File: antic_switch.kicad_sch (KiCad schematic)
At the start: 10 parts, among them J1 2.54, J2 2.00, P1 ANTIC_Conn, SW2 SW_Push_SPDT, U1 ANTIC_NTSC, U2 74LS245, U3 ANTIC_PAL, U4 74LS245

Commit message: gerber
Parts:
- SW2: now left out of the parts list
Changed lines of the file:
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@@
 		(unit 1)
 		(exclude_from_sim no)
-		(in_bom yes)
-		(on_board yes)
+		(in_bom no)
+		(on_board no)
 		(dnp no)
 		(property "Reference" "SW2"

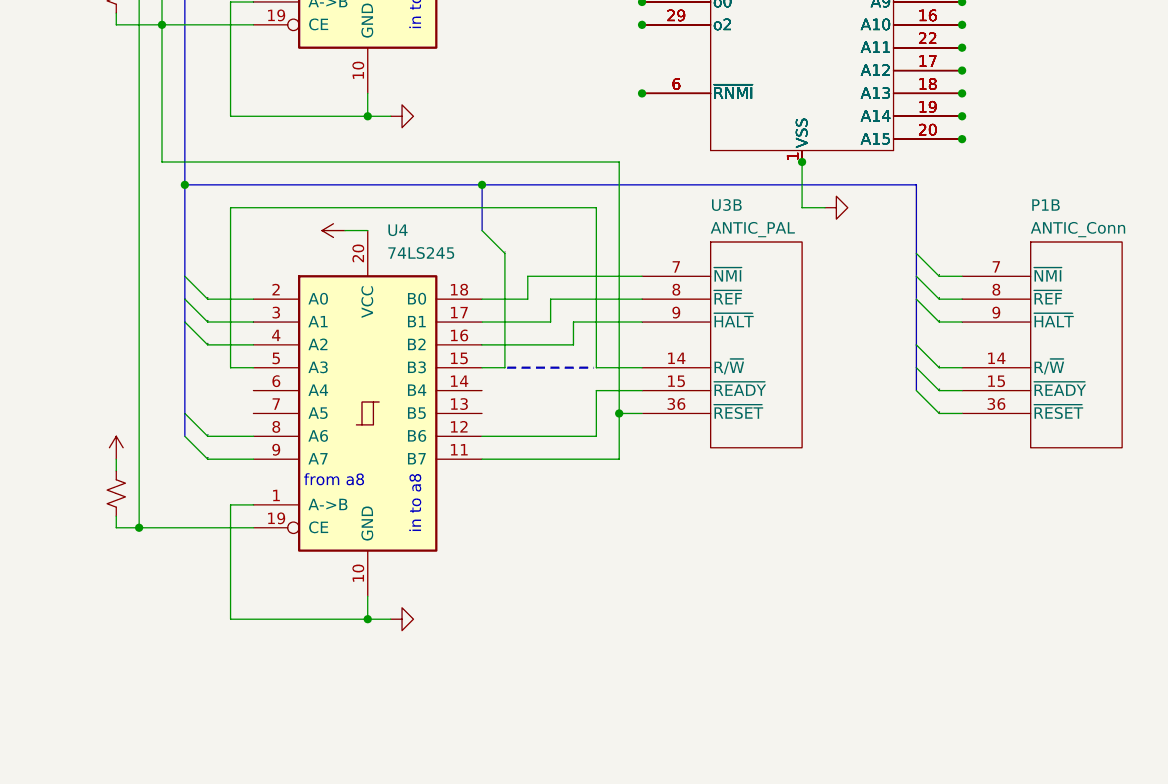
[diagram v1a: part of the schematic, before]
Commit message: header for gtia clocks
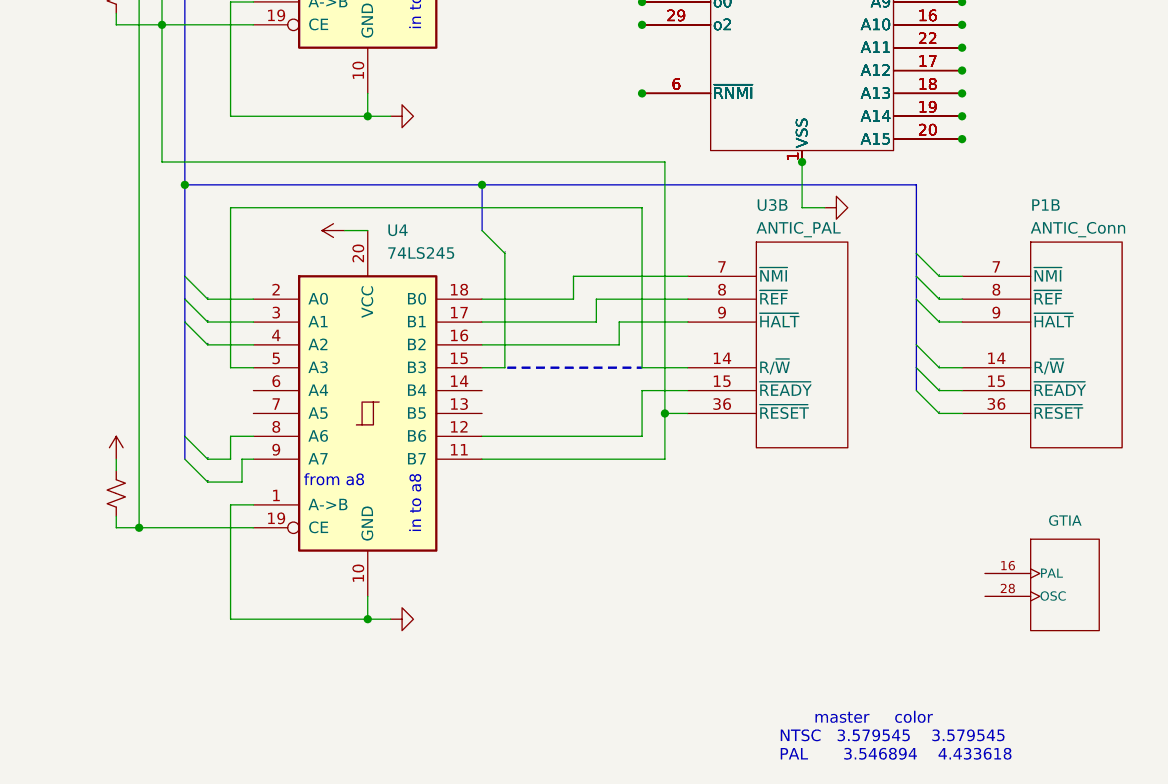
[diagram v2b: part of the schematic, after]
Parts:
- added IC2: GTIA, Package_DIP:DIP-40_W15.24mm, symbol Atari8:GTIA
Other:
- note added: "master color NTSC 3.579545 3.579545 PAL 3.546894 4.433618"
- moved on the sheet: U3B
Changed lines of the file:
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@@
 		)
 	)
+	(text "	   master 	color\nNTSC   3.579545	3.579545\nPAL	   3.546894	4.433618"
+		(exclude_from_sim no)
+		(at 177.8 157.734 0)
+		(effects
+			(font
+				(size 1.27 1.27)
+			)
+			(justify left top)
+		)
+	)
 	(text "in to a8"
 		(exclude_from_sim no)
@@
 	)
 	(junction
-		(at 160.02 124.46)
+		(at 165.1 124.46)
 		(diameter 0)
 		(color 0 0 0 0)
@@
 	)
 	(bus_entry
-		(at 111.76 124.46)
+		(at 111.76 127)
 		(size 2.54 2.54)
 		(stroke
@@
 	)
 	(bus_entry
-		(at 111.76 127)
+		(at 111.76 129.54)
 		(size 2.54 2.54)
 		(stroke
@@
 	(wire
 		(pts
-			(xy 152.4 114.3) (xy 144.78 114.3)
+			(xy 157.48 114.3) (xy 144.78 114.3)
 		)
 		(stroke
@@
 	(wire
 		(pts
-			(xy 157.48 101.6) (xy 116.84 101.6)
+			(xy 162.56 101.6) (xy 116.84 101.6)
 		)
 		(stroke
@@
 	(bus
 		(pts
-			(xy 111.76 114.3) (xy 111.76 124.46)
+			(xy 111.76 114.3) (xy 111.76 127)
 		)
 		(stroke
@@
 	(wire
 		(pts
-			(xy 154.94 116.84) (xy 144.78 116.84)
+			(xy 160.02 116.84) (xy 144.78 116.84)
 		)
 		(stroke
@@
 	(wire
 		(pts
-			(xy 160.02 96.52) (xy 160.02 124.46)
+			(xy 165.1 96.52) (xy 165.1 124.46)
 		)
 		(stroke
@@
 	(wire
 		(pts
-			(xy 157.48 119.38) (xy 162.56 119.38)
+			(xy 162.56 119.38) (xy 167.64 119.38)
 		)
 		(stroke
@@
 	(wire
 		(pts
-			(xy 160.02 129.54) (xy 160.02 124.46)
+			(xy 165.1 129.54) (xy 165.1 124.46)
 		)
 		(stroke
@@
 	(polyline
 		(pts
-			(xy 147.574 119.38) (xy 157.226 119.38)
+			(xy 147.574 119.38) (xy 162.56 119.38)
 		)
 		(stroke
@@
 	(wire
 		(pts
-			(xy 157.48 127) (xy 157.48 121.92)
+			(xy 162.56 127) (xy 162.56 121.92)
 		)
 		(stroke
@@
 	(wire
 		(pts
-			(xy 157.48 121.92) (xy 162.56 121.92)
+			(xy 162.56 121.92) (xy 167.64 121.92)
 		)
 		(stroke
@@
 	(wire
 		(pts
+			(xy 118.11 129.54) (xy 119.38 129.54)
+		)
+		(stroke
+			(width 0)
+			(type default)
+		)
+	)
+	(wire
+		(pts
 			(xy 144.78 63.5) (xy 147.32 63.5)
 		)
@@
 	(wire
 		(pts
-			(xy 157.48 119.38) (xy 157.48 101.6)
+			(xy 162.56 119.38) (xy 162.56 101.6)
 		)
 		(stroke
@@
 	(wire
 		(pts
-			(xy 114.3 127) (xy 119.38 127)
+			(xy 114.3 129.54) (xy 116.84 129.54)
 		)
 		(stroke
@@
 	(bus
 		(pts
-			(xy 111.76 124.46) (xy 111.76 127)
+			(xy 111.76 127) (xy 111.76 129.54)
 		)
 		(stroke
@@
 	(wire
 		(pts
-			(xy 162.56 111.76) (xy 152.4 111.76)
+			(xy 167.64 111.76) (xy 157.48 111.76)
 		)
 		(stroke
@@
 	(wire
 		(pts
-			(xy 152.4 111.76) (xy 152.4 114.3)
+			(xy 157.48 111.76) (xy 157.48 114.3)
 		)
 		(stroke
@@
 	(wire
 		(pts
-			(xy 144.78 127) (xy 157.48 127)
+			(xy 144.78 127) (xy 162.56 127)
 		)
 		(stroke
@@
 	(wire
 		(pts
-			(xy 114.3 129.54) (xy 119.38 129.54)
+			(xy 114.3 132.08) (xy 118.11 132.08)
 		)
 		(stroke
@@
 	(wire
 		(pts
-			(xy 162.56 109.22) (xy 149.86 109.22)
+			(xy 167.64 109.22) (xy 154.94 109.22)
 		)
 		(stroke
@@
 	(wire
 		(pts
-			(xy 149.86 109.22) (xy 149.86 111.76)
+			(xy 154.94 109.22) (xy 154.94 111.76)
 		)
 		(stroke
@@
 	(wire
 		(pts
+			(xy 116.84 127) (xy 119.38 127)
+		)
+		(stroke
+			(width 0)
+			(type default)
+		)
+	)
+	(wire
+		(pts
 			(xy 152.4 58.42) (xy 144.78 58.42)
 		)
@@
 	(wire
 		(pts
-			(xy 154.94 114.3) (xy 154.94 116.84)
+			(xy 160.02 114.3) (xy 160.02 116.84)
 		)
 		(stroke
@@
 	(wire
 		(pts
-			(xy 162.56 114.3) (xy 154.94 114.3)
+			(xy 167.64 114.3) (xy 160.02 114.3)
 		)
 		(stroke
@@
 	(wire
 		(pts
-			(xy 144.78 129.54) (xy 160.02 129.54)
+			(xy 144.78 129.54) (xy 165.1 129.54)
 		)
 		(stroke
@@
 	(wire
 		(pts
-			(xy 160.02 124.46) (xy 162.56 124.46)
+			(xy 165.1 124.46) (xy 167.64 124.46)
 		)
 		(stroke
@@
 	(wire
 		(pts
+			(xy 116.84 129.54) (xy 116.84 127)
+		)
+		(stroke
+			(width 0)
+			(type default)
+		)
+	)
+	(wire
+		(pts
 			(xy 133.35 19.05) (xy 133.35 38.1)
 		)
@@
 	(wire
 		(pts
-			(xy 144.78 111.76) (xy 149.86 111.76)
+			(xy 144.78 111.76) (xy 154.94 111.76)
+		)
+		(stroke
+			(width 0)
+			(type default)
+		)
+	)
+	(wire
+		(pts
+			(xy 118.11 132.08) (xy 118.11 129.54)
 		)
 		(stroke
@@
 	(wire
 		(pts
-			(xy 160.02 96.52) (xy 109.22 96.52)
+			(xy 165.1 96.52) (xy 109.22 96.52)
 		)
 		(stroke
@@
 	)
 	(label "~{READY}"
-		(at 114.3 127 0)
+		(at 114.3 129.54 0)
 		(effects
 			(font
@@
 	)
 	(label "~{RESET}"
-		(at 114.3 129.54 0)
+		(at 114.3 132.08 0)
 		(effects
 			(font
@@
 		(lib_name "ANTIC_4")
 		(lib_id "Atari8:ANTIC")
-		(at 180.34 54.61 0)
+		(at 185.42 54.61 0)
 		(unit 2)
 		(exclude_from_sim no)
@@
 		(dnp no)
 		(property "Reference" "U3"
-			(at 170.18 101.3459 0)
+			(at 175.26 101.3459 0)
 			(effects
 				(font
@@
 		)
 		(property "Value" "ANTIC_PAL"
-			(at 170.18 103.8859 0)
+			(at 175.26 103.8859 0)
 			(effects
 				(font
@@
 		)
 		(property "Footprint" ""
-			(at 198.12 100.33 0)
+			(at 203.2 100.33 0)
 			(effects
 				(font
@@
 		)
 		(property "Datasheet" ""
-			(at 180.34 54.61 0)
+			(at 185.42 54.61 0)
 			(effects
 				(font
@@
 		)
 		(property "Description" ""
-			(at 180.34 54.61 0)
+			(at 185.42 54.61 0)
 			(effects
 				(font
@@
 					(unit 1)
 				)
+			)
+		)
+	)
+	(symbol
+		(lib_id "Atari8:GTIA")
+		(at 209.55 142.24 0)
+		(unit 1)
+		(exclude_from_sim no)
+		(in_bom no)
+		(on_board no)
+		(dnp no)
+		(fields_autoplaced yes)
+		(property "Reference" "IC2"
+			(at 209.55 133.858 0)
+			(effects
+				(font
+					(size 1.143 1.143)
+				)
+				(hide yes)
+			)
+		)
+		(property "Value" "GTIA"
+			(at 209.55 136.398 0)
+			(effects
+				(font
+					(size 1.143 1.143)
+				)
+			)
+		)
+		(property "Footprint" "Package_DIP:DIP-40_W15.24mm"
+			(at 217.932 177.8 0)
+			(effects
+				(font
+					(size 0.508 0.508)
+				)
+				(hide yes)
+			)
+		)
+		(property "Datasheet" ""
+			(at 209.55 142.24 0)
+			(effects
+				(font
+					(size 1.27 1.27)
+				)
+				(hide yes)
+			)
+		)
+		(property "Description" ""
+			(at 209.55 142.24 0)
+			(effects
+				(font
+					(size 1.27 1.27)
+				)
+				(hide yes)
+			)
+		)
+		(pin "28"
+		)
+		(pin "27"
+		)
+		(pin "3"
+		)
+		(pin "16"
+		)
+		(instances
+			(project ""
+				(path "/4c615cf2-db67-4303-ba81-59c705659797"
+					(reference "IC2")
+					(unit 1)
+				)

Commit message: complete rework
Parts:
- J1: value 2.54 -> 2.54m
- J2: value 2.00 -> 2.00m
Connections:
- net R/~{W}: now also U2.12 (B6), U4.12 (B6); no longer P1.14 (R/~{W}), U2.15 (B3), U4.15 (B3)
- net ~{HALT}: now also U2.7 (A5), U4.7 (A5); no longer U2.4 (A2), U4.4 (A2)
- net ~{NMI}: now also U2.5 (A3), U4.5 (A3); no longer U2.2 (A0), U4.2 (A0)
- net ~{READY}: now also U2.9 (A7), U4.9 (A7); no longer U2.8 (A6), U4.8 (A6)
- net ~{REF}: now also U2.6 (A4), U4.6 (A4); no longer U2.3 (A1), U4.3 (A1)
- net ~{RESET}: now also U2.17 (B1), U4.17 (B1); no longer U2.9 (A7), U4.9 (A7)
- net at U1.14 (R/~{W}): now also P1.14 (R/~{W}), U3.14 (R/~{W}); no longer U2.5 (A3)
- net at U1.15 (~{READY}): now also U2.11 (B7); no longer U2.12 (B6)
- net at U1.7 (~{NMI}): now also U2.15 (B3); no longer U2.18 (B0)
- net at U1.8 (~{REF}): now also U2.14 (B4); no longer U2.17 (B1)
- net at U1.9 (~{HALT}): now also U2.13 (B5); no longer U2.16 (B2)
- net at U3.15 (~{READY}): now also U4.11 (B7); no longer U4.12 (B6)
- net at U4.13 (B5): now also U3.9 (~{HALT})
- net at U4.14 (B4): now also U3.8 (~{REF})
- net FI0: now reaches U4.16 (B2)
- net FI0: now also P1.35 (FI0), U2.16 (B2); no longer U3.9 (~{HALT})
- net at U3.7 (~{NMI}): now also U4.15 (B3); no longer U4.18 (B0)
- net at U3.14 (R/~{W}): no longer U4.5 (A3)
- net NTSC renamed ~{NTSC/P_OFF}
- net ~{NTSC/P_OFF}: now also U2.3 (A1); no longer U4.11 (B7)
- net PAL renamed ~{PAL/N_OFF}
- net ~{PAL/N_OFF}: now also U4.3 (A1); no longer U2.11 (B7)
- new net: U1.35 (FI0), U2.4 (A2)
- new net: U1.4 (~{LP}), U2.2 (A0)
- new net: U3.4 (~{LP}), U4.2 (A0)
- new net: U3.35 (FI0), U4.4 (A2)
- new net ~{LP}: P1.4 (~{LP}), U2.18 (B0), U4.18 (B0)
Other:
- note added: "SIGNAL DIRECTION NOTES --------- LP - IN to antic RNMI - IN to antic (held high) NMI - OUT to cpu REF - OUT to computer HALT - OUT to cpu (read memory) R/W - IN or Bi-dir, unsure RDY - OUT to cpu (WSYNC) FI0 - IN clk from gtia o2 - OUT clk to cpu (buffered, U18D) o0 - IN clk from cpu (buffered, U18B) RST - IN from computer"
- note removed: "from a8"
- note removed: "in to a8"
- moved on the sheet: SW2, U1, U2, U4
